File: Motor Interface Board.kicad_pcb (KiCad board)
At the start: 2 copper layers, 71.3 x 44.6 mm, 17 parts, among them J1 Conn_02x05_Odd_Even, J2 Conn_02x05_Odd_Even, J3 Conn_01x02_Pin, J4 Conn_01x02_Pin, J5 Conn_01x20, J6 Conn_01x20, J7 Conn_02x04_Odd_Even, U1 TXB0108PW

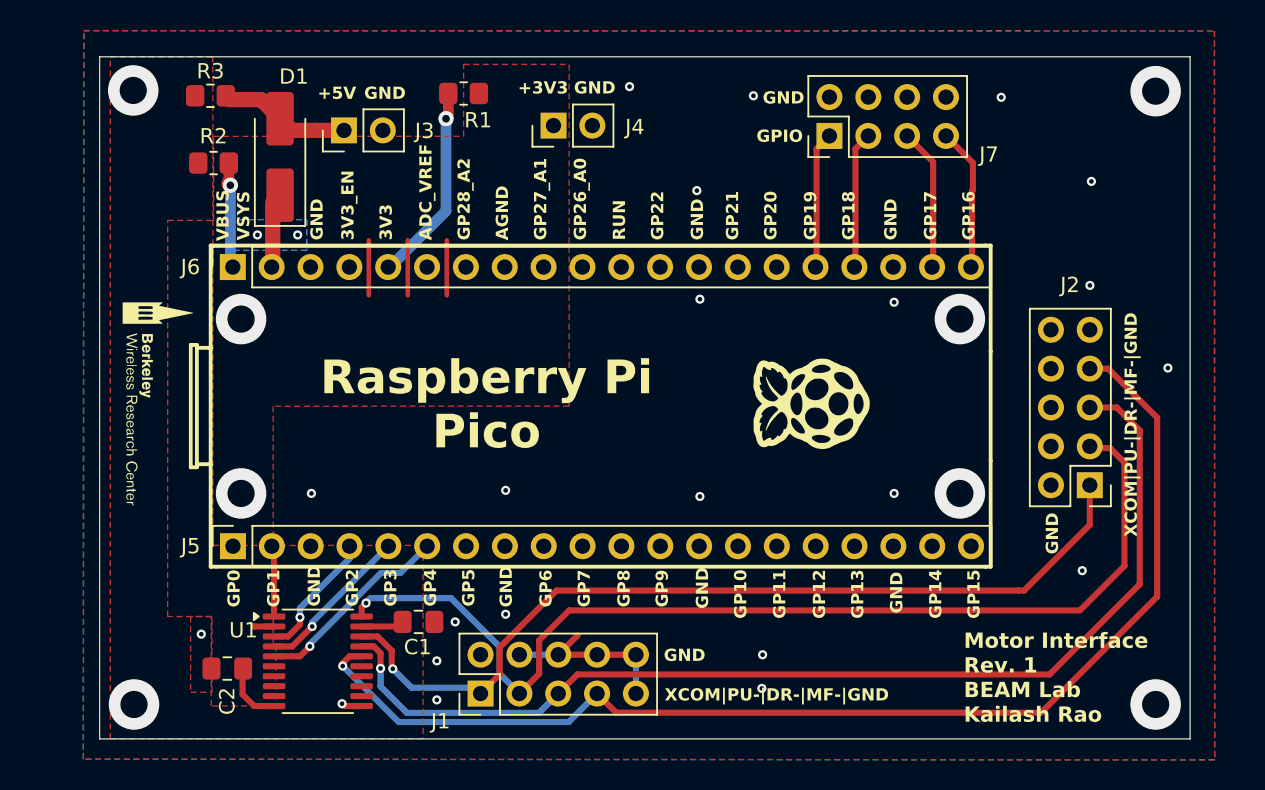
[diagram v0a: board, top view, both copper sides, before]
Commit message: Update mounting hole vias
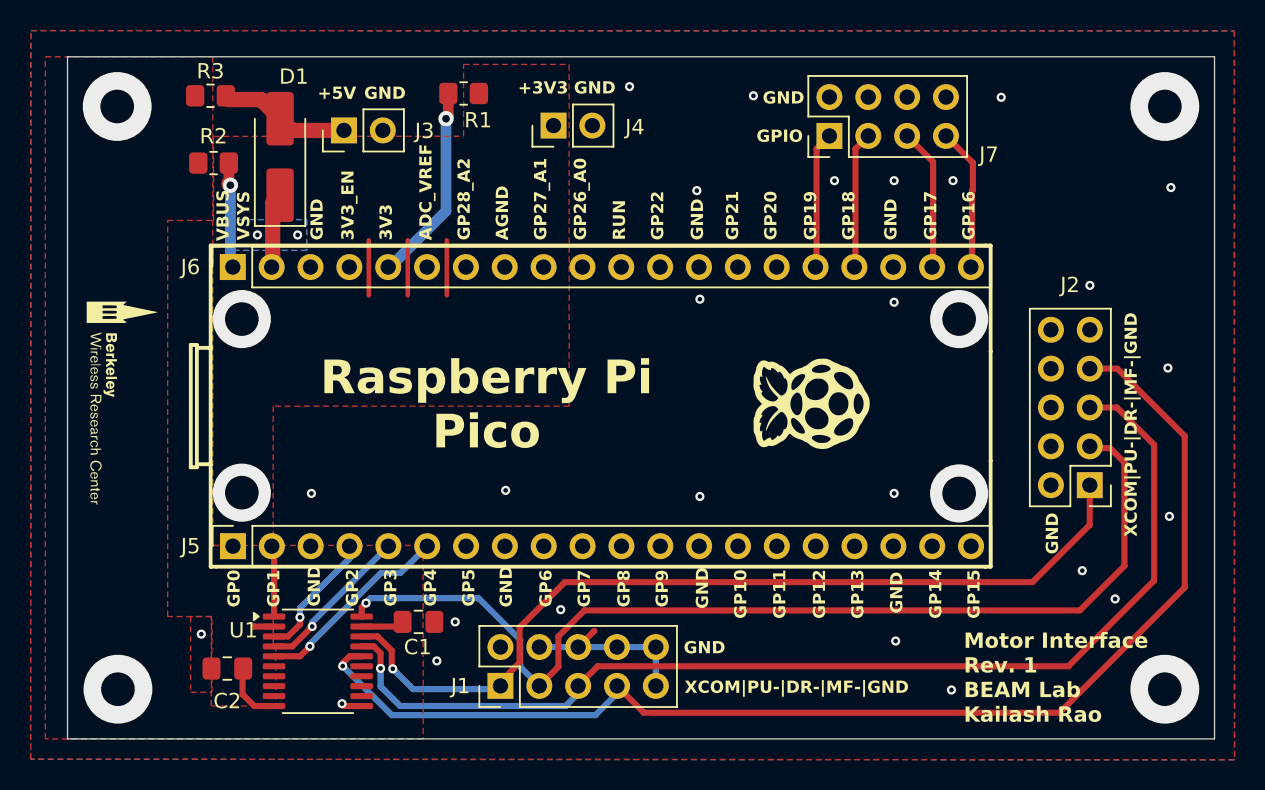
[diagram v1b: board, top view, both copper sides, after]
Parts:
- moved G*** 2.35 mm to (146.4, 52.2)
- moved J1 1.39 mm to (171.0, 70.8)
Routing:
- net /MF-: track 78.3 -> 80.6 mm
- net /XCOM: track 58.2 -> 58.9 mm
- net /DR-: track 71.4 -> 72.0 mm
- net /PU-: track 68.6 -> 68.1 mm
- net GND: track 13.3 -> 13.0 mm, vias 30 -> 34
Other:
- board size 71.3 x 44.6 mm -> 75 x 44.6 mm
